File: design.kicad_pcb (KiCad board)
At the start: 2 copper layers, 80 x 55 mm, 80 parts, among them J1 2601-3108, J10 Conn_01x04, J11 Conn_01x04, J12 Conn_01x03, J13 Conn_01x03, J14 BM04B-SRSS-TB_LF__SN_, J2 2601-3108, J3 2601-3108, J4 TYPE-C-31-M-12, J5 SKEDD-UPDI-4, J6 Conn_01x04, J7 Conn_01x04, J8 Conn_01x04, J9 Conn_01x04, U1 ATtiny1616-S, U2 AP2112K-3.3, U3 CP2105

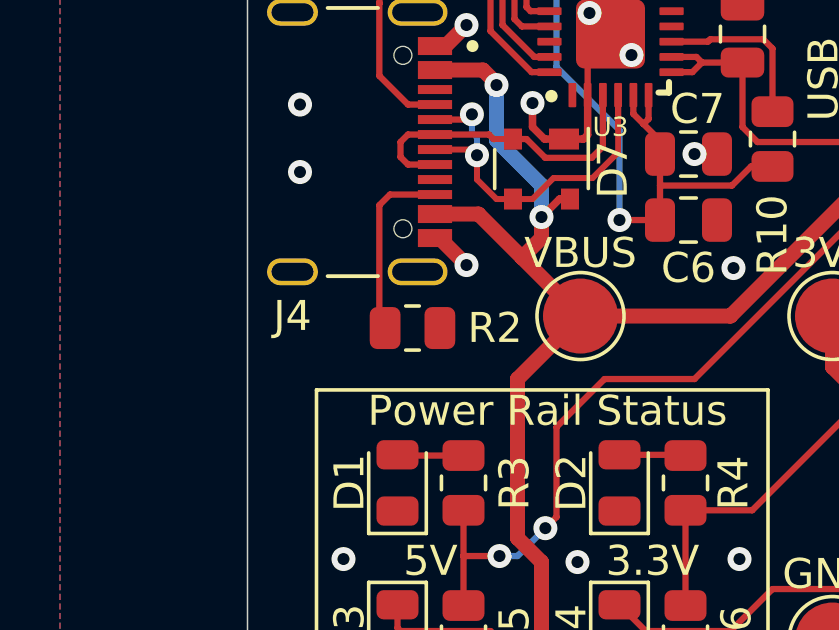
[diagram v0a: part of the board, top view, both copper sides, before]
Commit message: align R1/R2 around USB connector
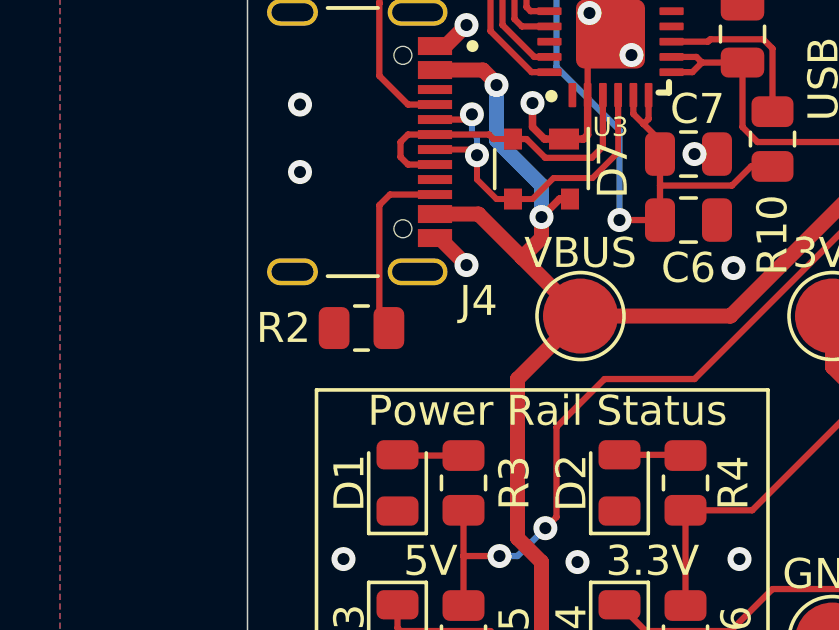
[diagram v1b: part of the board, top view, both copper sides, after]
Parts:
- moved R2 1.70 mm to (91.3, 90.9), turned to 180 degrees
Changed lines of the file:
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@@
     (property "SnapEDA_Link" "https://www.snapeda.com/parts/TYPE-C-31-M-12/HRO+Electronics+Co.%252C+Ltd./view-part/?ref=snap")
     (attr smd)
-    (fp_text reference "J4" (at 5.8 0 180) (layer "F.SilkS")
+    (fp_text reference "J4" (at 5.3 -6.2 180) (layer "F.SilkS")
       (effects (font (size 1 1) (thickness 0.15)))
     )
@@
   )
   (footprint "Resistor_SMD:R_0805_2012Metric" (layer "F.Cu")
-    (at 93 90.9)
+    (at 91.3 90.9 180)
     (descr "Resistor SMD 0805 (2012 Metric), square (rectangular) end terminal, IPC_7351 nominal, (Body size source: IPC-SM-782 page 72, https://www.pcb-3d.com/wordpress/wp-content/uploads/ipc-sm-782a_amendment_1_and_2.pdf), generated with kicad-footprint-generator")
     (tags "resistor")
@@
     (property "Sheetname" "")
     (attr smd)
-    (fp_text reference "R2" (at 2.75 0) (layer "F.SilkS")
+    (fp_text reference "R2" (at 2.6 0) (layer "F.SilkS")
       (effects (font (size 1 1) (thickness 0.15)))
     )
@@
     (fp_line (start 1 -0.625) (end 1 0.625) (layer "F.Fab") (width 0.1))
     (fp_line (start -1 -0.625) (end 1 -0.625) (layer "F.Fab") (width 0.1))
-    (pad "1" smd roundrect (at -0.9125 0) (size 1.025 1.4) (layers "F.Cu" "F.Paste" "F.Mask") (roundrect_rratio 0.243902)
+    (pad "1" smd roundrect (at -0.9125 0 180) (size 1.025 1.4) (layers "F.Cu" "F.Paste" "F.Mask") (roundrect_rratio 0.243902)
       (net 42 "Net-(J4-PadB5)") (pintype "passive"))
-    (pad "2" smd roundrect (at 0.9125 0) (size 1.025 1.4) (layers "F.Cu" "F.Paste" "F.Mask") (roundrect_rratio 0.243902)
+    (pad "2" smd roundrect (at 0.9125 0 180) (size 1.025 1.4) (layers "F.Cu" "F.Paste" "F.Mask") (roundrect_rratio 0.243902)
       (net 32 "GND") (pintype "passive"))
     (model "${KICAD6_3DMODEL_DIR}/Resistor_SMD.3dshapes/R_0805_2012Metric.wrl"

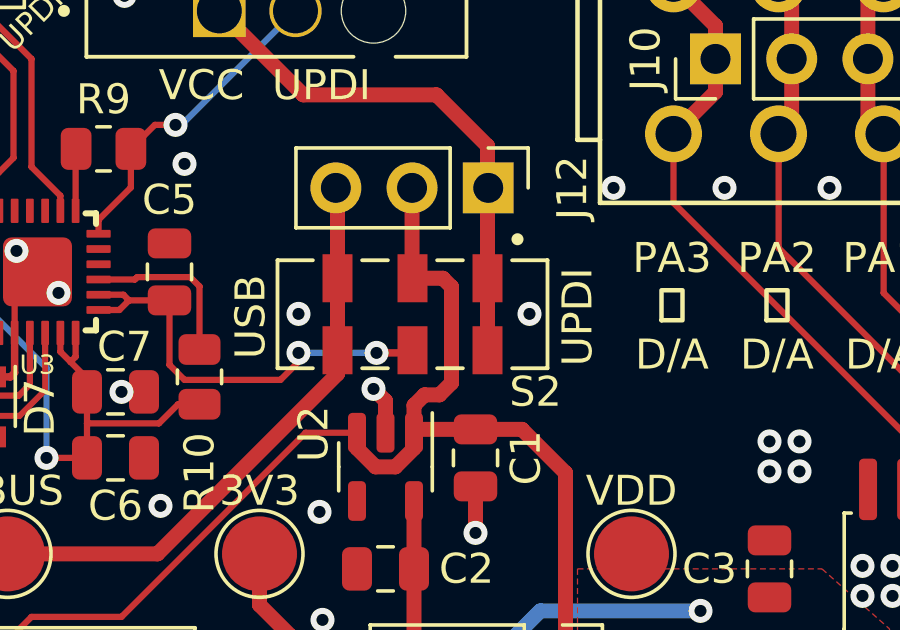
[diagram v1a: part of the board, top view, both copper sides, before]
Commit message: correct DRC issues
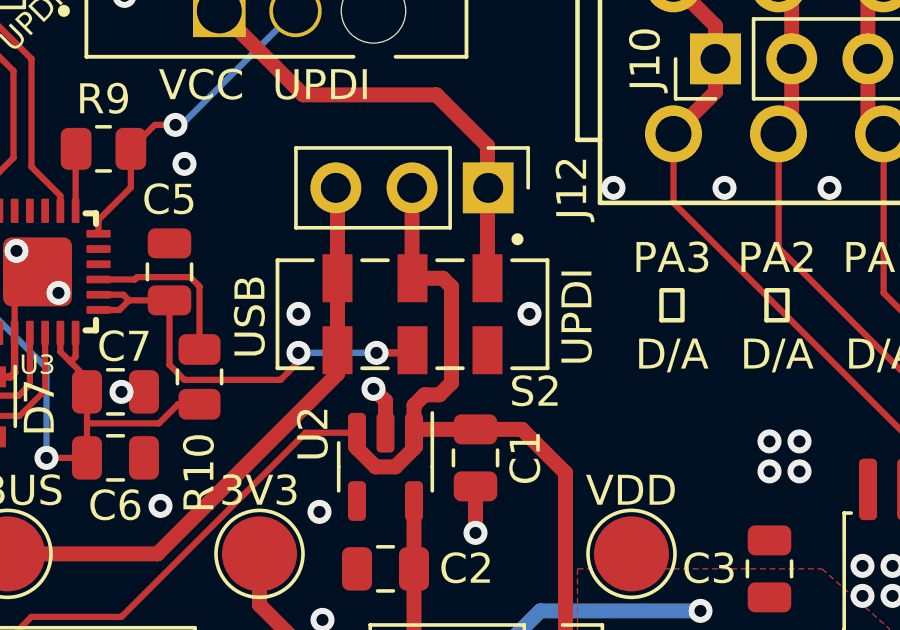
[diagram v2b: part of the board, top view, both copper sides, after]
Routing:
- net VCC: track 17.6 -> 15.2 mm
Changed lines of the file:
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@@
   (segment (start 114.6 81.3125) (end 114.6 76.9) (width 0.5) (layer "F.Cu") (net 45))
   (segment (start 112.9 75.2) (end 108.46 75.2) (width 0.5) (layer "F.Cu") (net 45))
-  (segment (start 114.6 81.3125) (end 114.6 83.7125) (width 0.5) (layer "F.Cu") (net 45))
   (segment (start 114.6 76.9) (end 112.9 75.2) (width 0.5) (layer "F.Cu") (net 45))
   (segment (start 108.46 75.2) (end 105.66 72.4) (width 0.5) (layer "F.Cu") (net 45))
@@
   (segment (start 102.65 82.05) (end 104 82.05) (width 0.21) (layer "F.Cu") (net 78))
   (segment (start 104 84.2) (end 104.5 84.7) (width 0.21) (layer "F.Cu") (net 78))
-  (segment (start 112.15 83.7625) (end 112.1 83.7125) (width 0.5) (layer "F.Cu") (net 78))
   (segment (start 107.7 84.7) (end 108.3 84.1) (width 0.21) (layer "F.Cu") (net 78))
   (segment (start 101.635 82.37) (end 102.33 82.37) (width 0.21) (layer "F.Cu") (net 78))

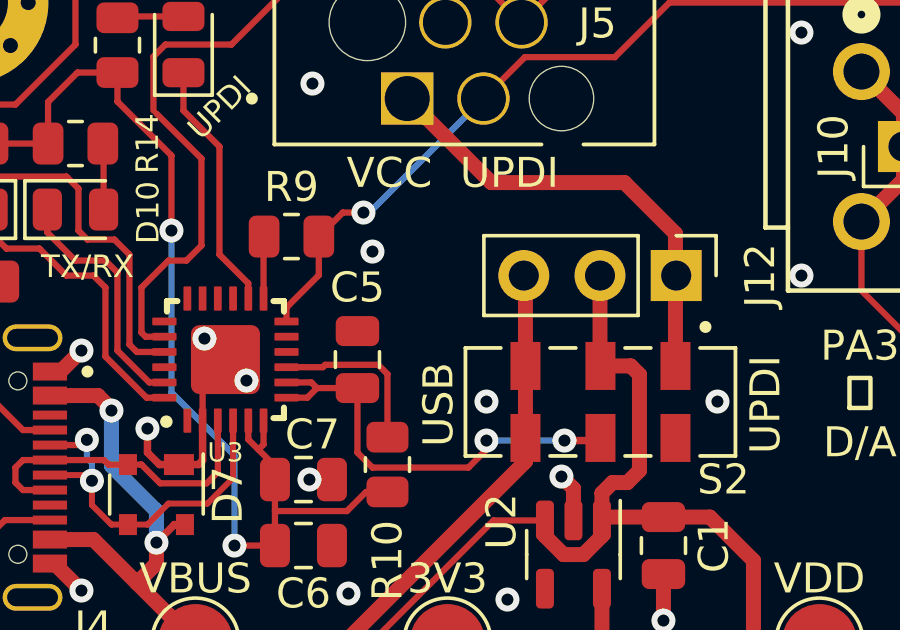
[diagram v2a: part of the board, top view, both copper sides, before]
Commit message: add CP2105 VBus solderbridge
closes #5
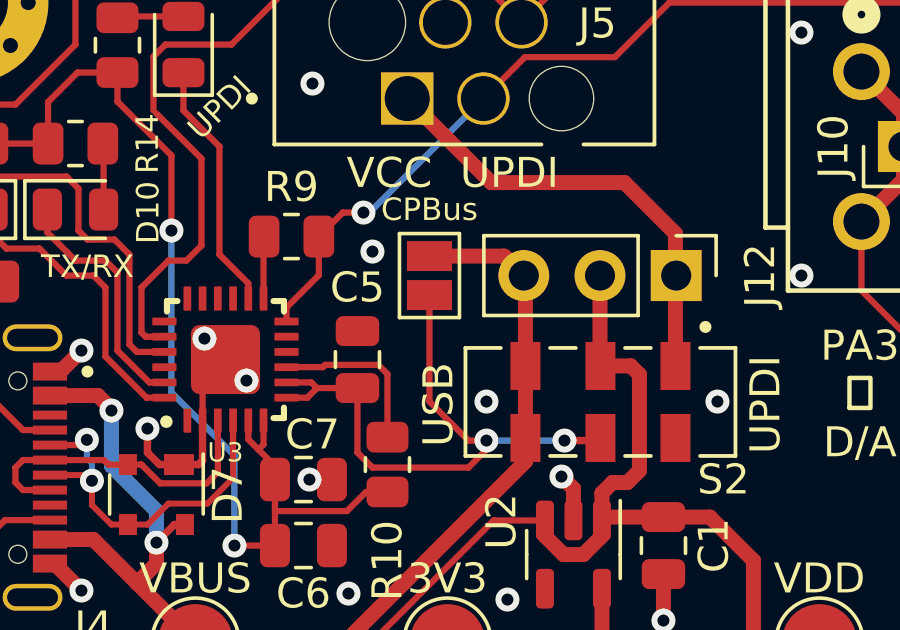
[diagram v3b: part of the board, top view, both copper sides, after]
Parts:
- added JP5: CPBus, Jumper:SolderJumper-2_P1.3mm_Open_Pad1.0x1.5mm, F.Cu at (106.4, 78.3)
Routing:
- net V_CP2105: track 14.3 -> 20.3 mm
- net VBUS: track 63.7 -> 67.1 mm
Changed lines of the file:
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@@
       (net 31 "VBUS") (pintype "passive") (solder_mask_margin 0.102))
     (pad "5" smd rect (at 1.2 -2.5 270) (size 1.6 1) (layers "F.Cu" "F.Paste" "F.Mask")
-      (net 79 "unconnected-(S2-Pad5)") (pintype "passive") (solder_mask_margin 0.102))
+      (net 79 "unconnected-(S2-Pad5)") (pintype "passive+no_connect") (solder_mask_margin 0.102))
     (pad "6" smd rect (at 1.2 0 270) (size 1.6 1) (layers "F.Cu" "F.Paste" "F.Mask")
       (net 78 "V_CP2105") (pintype "passive") (solder_mask_margin 0.102))
@@
     )
   )
+  (footprint "Jumper:SolderJumper-2_P1.3mm_Open_Pad1.0x1.5mm" (layer "F.Cu")
+    (at 106.4 78.3 -90)
+    (descr "SMD Solder Jumper, 1x1.5mm Pads, 0.3mm gap, open")
+    (tags "solder jumper open")
+    (property "Sheetfile" "design.kicad_sch")
+    (property "Sheetname" "")
+    (attr exclude_from_pos_files)
+    (fp_text reference "JP5" (at 0 -1.8 90) (layer "F.SilkS") hide
+      (effects (font (size 1 1) (thickness 0.15)))
+    )
+    (fp_text value "CPBus" (at -2.2 0 180) (layer "F.SilkS")
+      (effects (font (size 0.75 0.75) (thickness 0.12)))
+    )
+    (fp_line (start -1.4 -1) (end 1.4 -1) (layer "F.SilkS") (width 0.12))
+    (fp_line (start 1.4 -1) (end 1.4 1) (layer "F.SilkS") (width 0.12))
+    (fp_line (start 1.4 1) (end -1.4 1) (layer "F.SilkS") (width 0.12))
+    (fp_line (start -1.4 1) (end -1.4 -1) (layer "F.SilkS") (width 0.12))
+    (fp_line (start 1.65 1.25) (end -1.65 1.25) (layer "F.CrtYd") (width 0.05))
+    (fp_line (start 1.65 1.25) (end 1.65 -1.25) (layer "F.CrtYd") (width 0.05))
+    (fp_line (start -1.65 -1.25) (end 1.65 -1.25) (layer "F.CrtYd") (width 0.05))
+    (fp_line (start -1.65 -1.25) (end -1.65 1.25) (layer "F.CrtYd") (width 0.05))
+    (pad "1" smd rect (at -0.65 0 270) (size 1 1.5) (layers "F.Cu" "F.Mask")
+      (net 31 "VBUS") (pinfunction "A") (pintype "passive"))
+    (pad "2" smd rect (at 0.65 0 270) (size 1 1.5) (layers "F.Cu" "F.Mask")
+      (net 78 "V_CP2105") (pinfunction "B") (pintype "passive"))
+  )
   (footprint "Resistor_SMD:R_0805_2012Metric" (layer "F.Cu")
     (at 91.3 90.9 180)
@@
   (segment (start 97.9 86.6) (end 98.25 86.6) (width 0.25) (layer "F.Cu") (net 31))
   (segment (start 97.3 108.129905) (end 97.3 98.7) (width 0.5) (layer "F.Cu") (net 31))
+  (segment (start 108.895 77.65) (end 106.4 77.65) (width 0.5) (layer "F.Cu") (net 31))
   (segment (start 99.095096 109.925001) (end 97.3 108.129905) (width 0.5) (layer "F.Cu") (net 31))
   (segment (start 95.35 82.3) (end 95.75 82.7) (width 0.5) (layer "F.Cu") (net 31))
   (segment (start 97.3 87.9) (end 97.3 87.2) (width 0.5) (layer "F.Cu") (net 31))
   (segment (start 95.75 82.75) (end 95.8 82.8) (width 0.5) (layer "F.Cu") (net 31))
+  (segment (start 109.545 78.3) (end 108.895 77.65) (width 0.5) (layer "F.Cu") (net 31))
   (segment (start 97.3 98.7) (end 96.5 97.9) (width 0.5) (layer "F.Cu") (net 31))
   (segment (start 100.58 113.440097) (end 99.095096 114.925001) (width 0.5) (layer "F.Cu") (net 31))
@@
   (segment (start 102.65 82.05) (end 104 82.05) (width 0.21) (layer "F.Cu") (net 78))
   (segment (start 104 84.2) (end 104.5 84.7) (width 0.21) (layer "F.Cu") (net 78))
+  (segment (start 106.4 82.5) (end 107.7 83.8) (width 0.21) (layer "F.Cu") (net 78))
+  (segment (start 107.7 83.8) (end 108.3 83.8) (width 0.21) (layer "F.Cu") (net 78))
   (segment (start 107.7 84.7) (end 108.3 84.1) (width 0.21) (layer "F.Cu") (net 78))
   (segment (start 101.635 82.37) (end 102.33 82.37) (width 0.21) (layer "F.Cu") (net 78))
   (segment (start 104.5 84.7) (end 107.7 84.7) (width 0.21) (layer "F.Cu") (net 78))
+  (segment (start 106.4 78.95) (end 106.4 82.5) (width 0.21) (layer "F.Cu") (net 78))
   (via (at 108.3 83.8) (size 0.8) (drill 0.4) (layers "F.Cu" "B.Cu") (net 78))
   (via (at 110.9 83.8) (size 0.8) (drill 0.4) (layers "F.Cu" "B.Cu") (net 78))

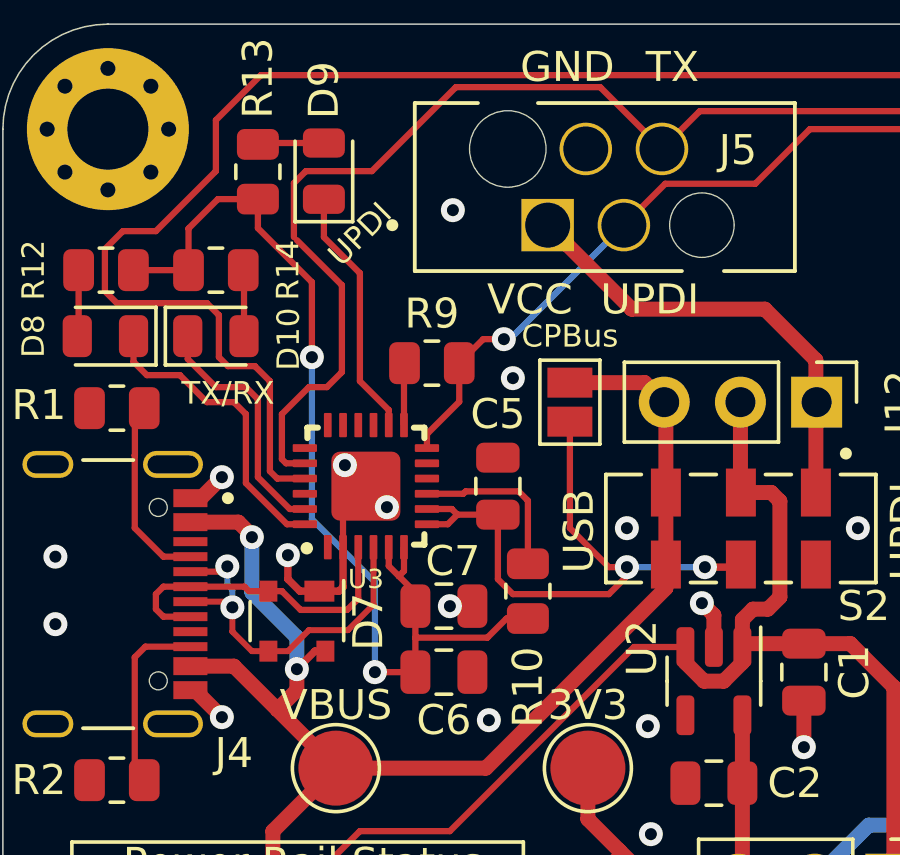
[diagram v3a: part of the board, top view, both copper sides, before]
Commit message: add programming capacitor
closes #4
to use the TX/RX LEDs the cp2105 must be programmed to use this function (only one time possible). Todo this a 4,7uF capacitor must be used on pin VPP according to the Datasheet Note 4 page 18.
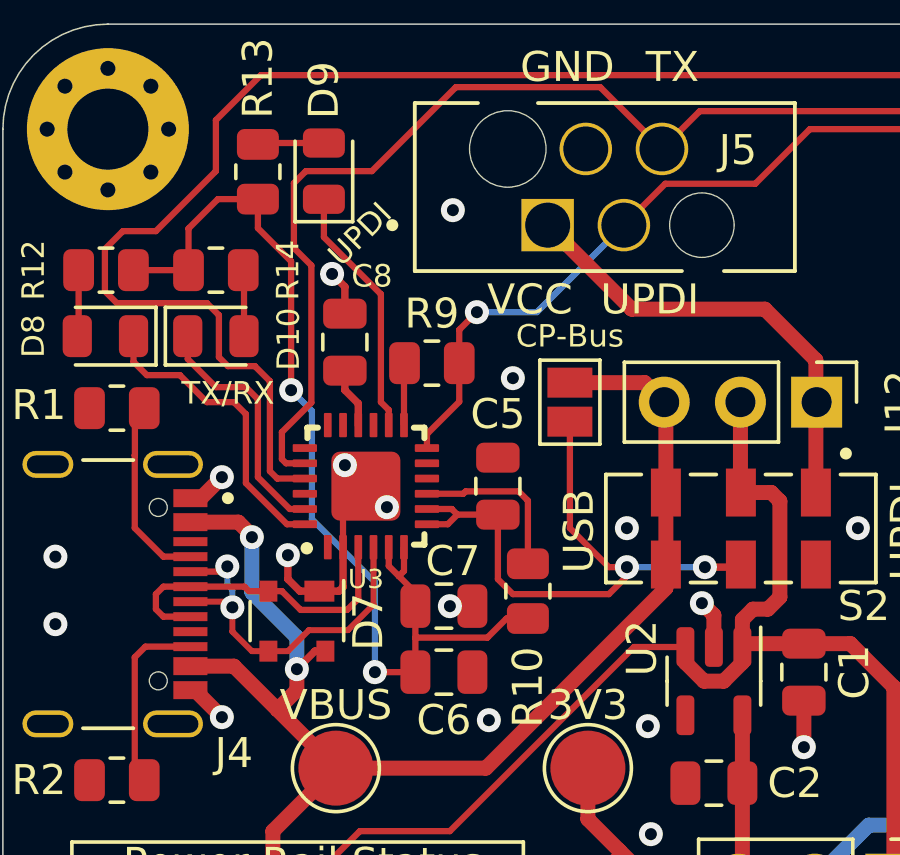
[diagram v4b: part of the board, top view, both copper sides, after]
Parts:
- added C8: 4,7uF, Capacitor_SMD:C_0805_2012Metric, F.Cu at (98.9, 76.3)
- JP5: value CPBus -> CP-Bus
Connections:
- U3 pad 16: unconnected-(U3-Pad16) -> Net-(U3-Pad16)
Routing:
- net Net-(U3-Pad16): track 0.00 -> 2.00 mm
- net GND: track 34.1 -> 35.6 mm, vias 68 -> 69
- net PB2: track 110.0 -> 108.9 mm
- net PA0: track 54.6 -> 55.2 mm

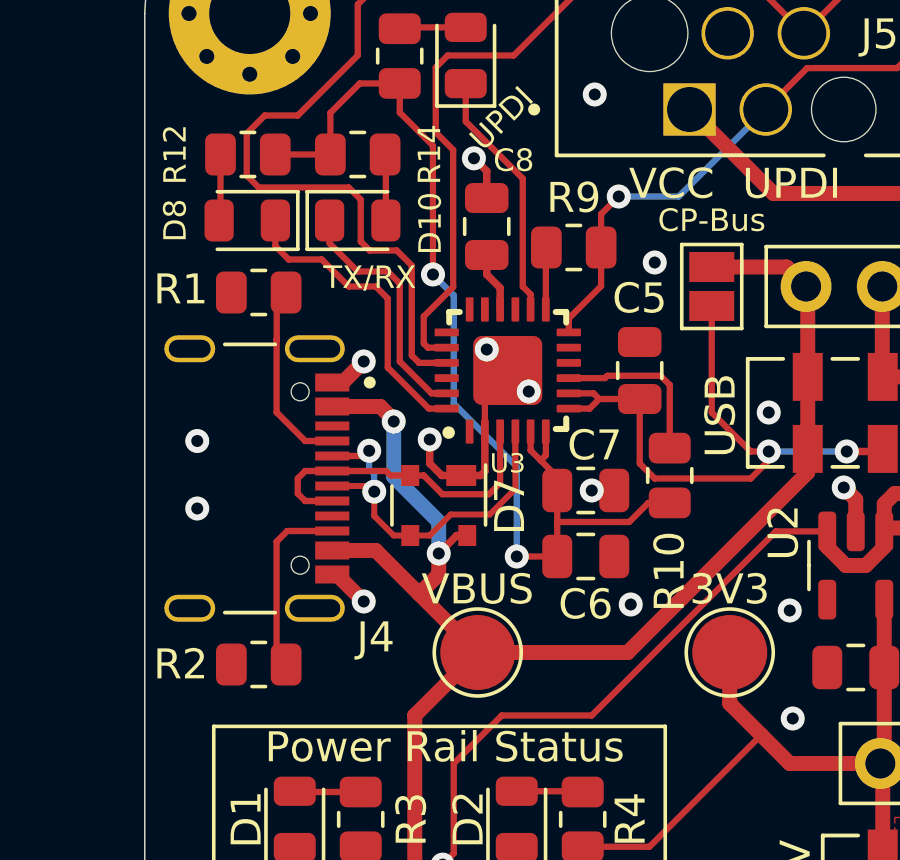
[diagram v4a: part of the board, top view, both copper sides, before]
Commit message: Add USB Programming interface
Touchpoints on Back for USB, Power and VPP.
VPP so the 4,7uF capacitor must not be populated and can be done with a programming rig.
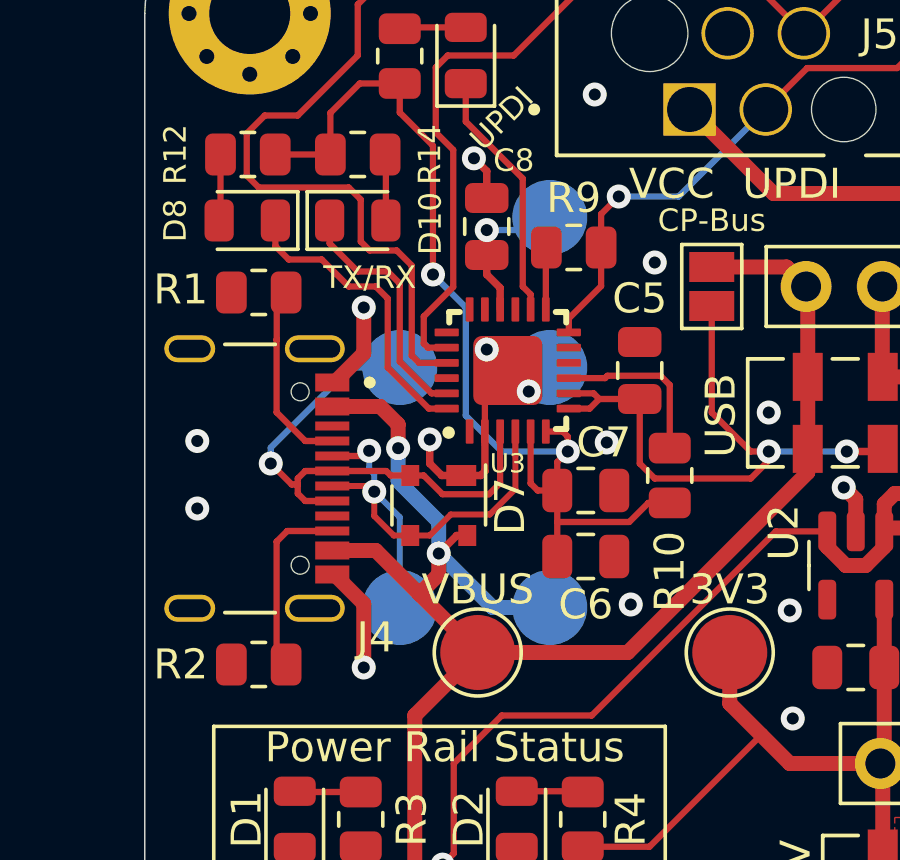
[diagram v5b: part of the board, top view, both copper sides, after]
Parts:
- added TP10: D+, TestPoint:TestPoint_Pad_D2.5mm, B.Cu at (96.0, 81.0)
- added TP11: D-, TestPoint:TestPoint_Pad_D2.5mm, B.Cu at (96.0, 89.0)
- added TP12: VPP, TestPoint:TestPoint_Pad_D2.5mm, B.Cu at (101.0, 76.0)
- added TP8: GND, TestPoint:TestPoint_Pad_D2.5mm, B.Cu at (101.0, 81.0)
- added TP9: VBUS, TestPoint:TestPoint_Pad_D2.5mm, B.Cu at (101.0, 89.0)
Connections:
- net Net-(U3-Pad16) renamed VPP
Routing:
- net D+: track 10.8 -> 17.9 mm, vias 0 -> 1
- net VBUS: track 67.1 -> 71.6 mm
- net D-: track 12.6 -> 16.8 mm
- net GND: track 35.6 -> 39.4 mm
- net VPP: track 2.00 -> 5.10 mm, vias 0 -> 1
- net VIO: track 34.3 -> 33.5 mm
